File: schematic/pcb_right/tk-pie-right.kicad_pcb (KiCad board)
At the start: 2 copper layers, 129 x 77.5 mm, 26 parts, among them J1 UART, J2 DBG

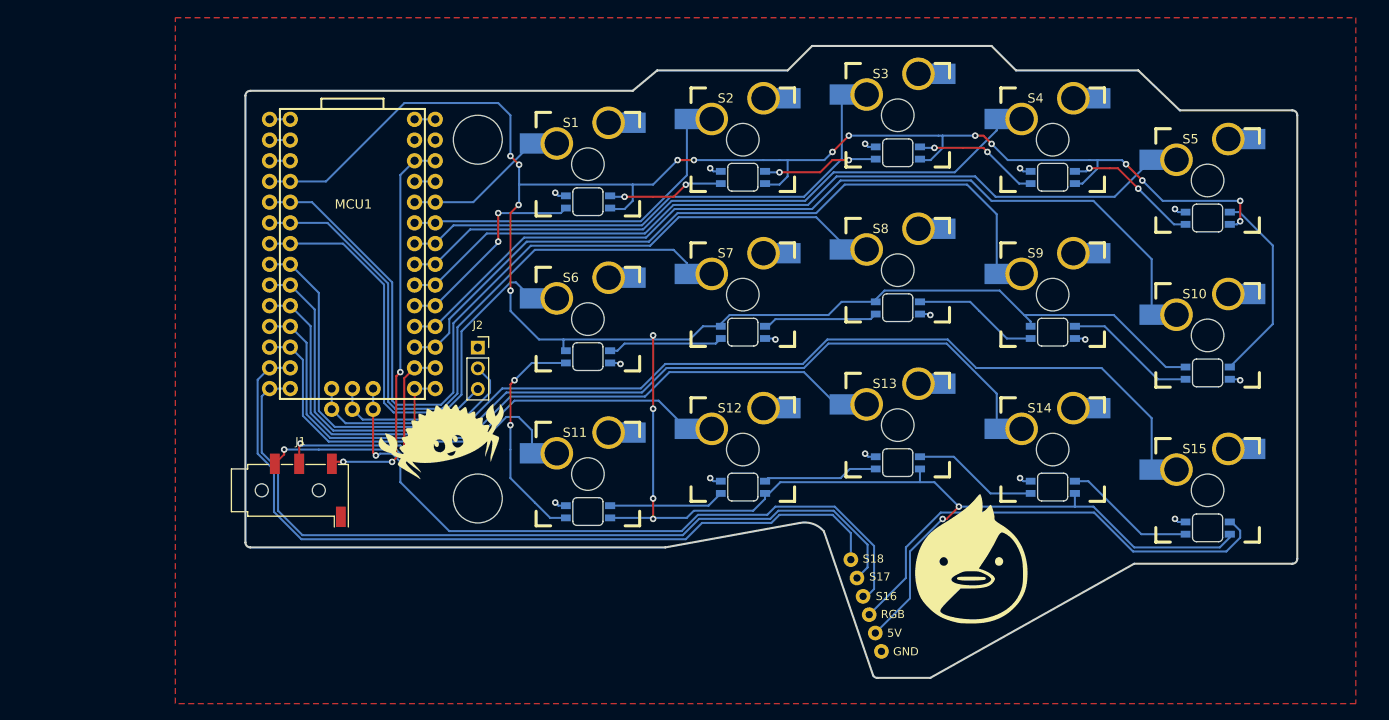
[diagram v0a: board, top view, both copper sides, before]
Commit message: Copy tk-pie-left to right and auto-flip it
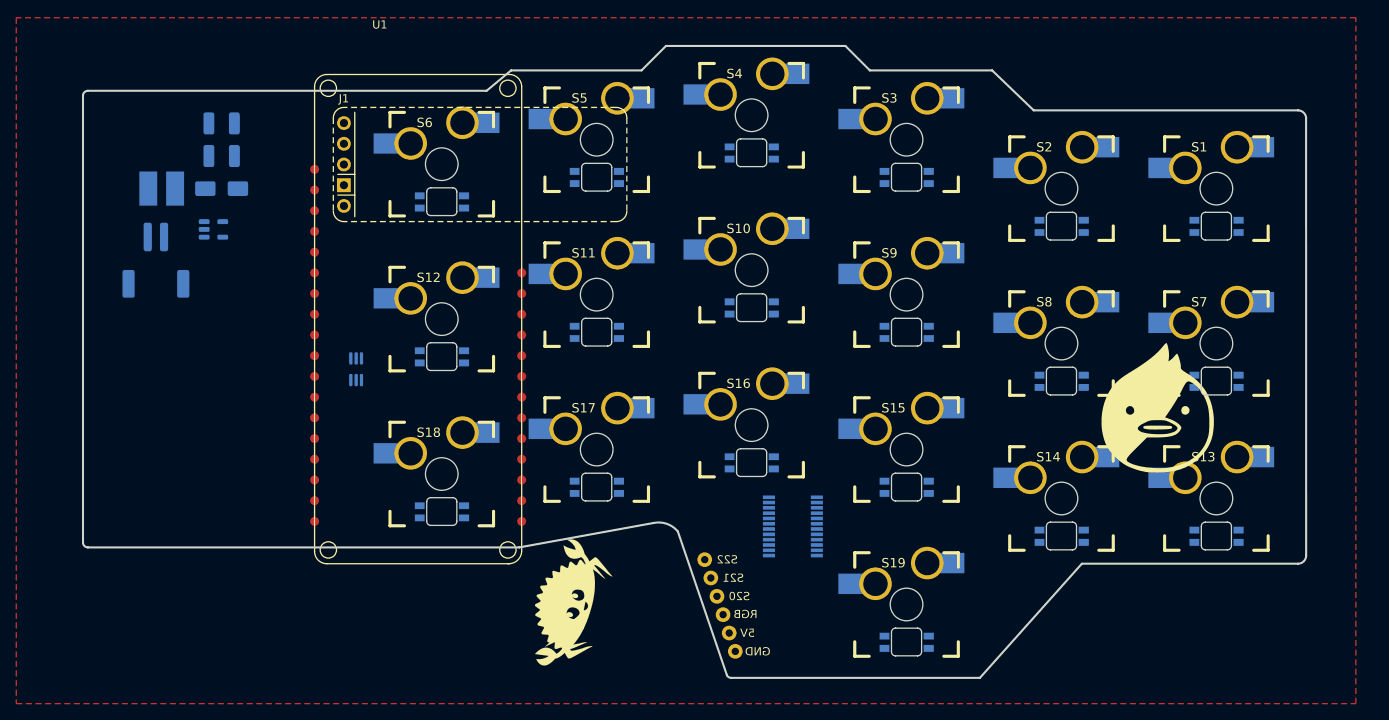
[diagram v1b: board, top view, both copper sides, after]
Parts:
- removed MCU1: ITSYBITSY RP2040, Footprints:ITSYBITSY BREAKOUT
- removed REF** (x2): MountingHole_6mm, MountingHole:MountingHole_6mm
- added C4: 12µF, Capacitor_SMD:C_1210_3225Metric_Pad1.33x2.70mm_HandSolder, B.Cu at (25.1, 35.0)
- added C5: 12µF, Capacitor_SMD:C_1210_3225Metric_Pad1.33x2.70mm_HandSolder, B.Cu at (25.1, 31.0)
- added D1: SS14, Diode_SMD:D_SMA, B.Cu at (25.1, 39.0)
- added IC1: PCA9539PW,118, Footprints:SOP65P640X110-24N, B.Cu at (95.1, 80.4)
- added L2: 22µH, Inductor_SMD:L_Cenker_CKCS5040, B.Cu at (17.7, 39.0)
- added PS1: ME2108C50M5G, Package_TO_SOT_SMD:SOT-23-5, B.Cu at (24.1, 44.0)
- added S1: MX_SW_SOCKET_LED, Footprints:MX_SW_SOCKET_LED, F.Cu at (147.1, 39.0)
- added S13: MX_SW_SOCKET_LED, Footprints:MX_SW_SOCKET_LED, F.Cu at (147.1, 77.0)
- added S19: MX_SW_SOCKET_RGB_REV, Footprints:MX_SW_SOCKET_LED_REV, F.Cu at (109.1, 90.0)
- added S7: MX_SW_SOCKET_RGB_REV, Footprints:MX_SW_SOCKET_LED_REV, F.Cu at (147.1, 58.0)
- added U1: ~, Footprints:DFR1075, F.Cu at (36.5, 25.0)
- added U3: SN74LVC1T45DCK, Package_TO_SOT_SMD:SOT-363_SC-70-6_Handsoldering, B.Cu at (41.6, 61.1)
- J1: value UART -> NiceView; footprint Connector_Audio:Jack_3.5mm_KoreanHropartsElec_PJ-320D-4A_Horizontal -> Footprints:Nice!View Header
- J2: value DBG -> Battery Connector; footprint Connector_PinSocket_2.54mm:PinSocket_1x03_P2.54mm_Vertical -> Connector_JST:JST_PH_S2B-PH-SM4-TB_1x02-1MP_P2.00mm_Horizontal; moved to B.Cu
- S10: renamed from S8; footprint Footprints:MX_SW_SOCKET_LED -> Footprints:MX_SW_SOCKET_LED_REV
- S11: renamed from S9; footprint Footprints:MX_SW_SOCKET_LED -> Footprints:MX_SW_SOCKET_LED_REV
- S12: renamed from S10; footprint Footprints:MX_SW_SOCKET_LED -> Footprints:MX_SW_SOCKET_LED_REV
- S14: renamed from S11; footprint Footprints:MX_SW_SOCKET_LED_REV -> Footprints:MX_SW_SOCKET_LED
- S15: renamed from S12; footprint Footprints:MX_SW_SOCKET_LED_REV -> Footprints:MX_SW_SOCKET_LED
- S16: renamed from S13; footprint Footprints:MX_SW_SOCKET_LED_REV -> Footprints:MX_SW_SOCKET_LED
- S17: renamed from S14; footprint Footprints:MX_SW_SOCKET_LED_REV -> Footprints:MX_SW_SOCKET_LED
- S18: renamed from S15; footprint Footprints:MX_SW_SOCKET_LED_REV -> Footprints:MX_SW_SOCKET_LED
- S2: renamed from S1; footprint Footprints:MX_SW_SOCKET_LED_REV -> Footprints:MX_SW_SOCKET_LED
- S3: renamed from S2; footprint Footprints:MX_SW_SOCKET_LED_REV -> Footprints:MX_SW_SOCKET_LED
- S4: renamed from S3; footprint Footprints:MX_SW_SOCKET_LED_REV -> Footprints:MX_SW_SOCKET_LED
- S5: renamed from S4; footprint Footprints:MX_SW_SOCKET_LED_REV -> Footprints:MX_SW_SOCKET_LED
- S6: renamed from S5; footprint Footprints:MX_SW_SOCKET_LED_REV -> Footprints:MX_SW_SOCKET_LED
- S8: renamed from S6; footprint Footprints:MX_SW_SOCKET_LED -> Footprints:MX_SW_SOCKET_LED_REV
- S9: renamed from S7; footprint Footprints:MX_SW_SOCKET_LED -> Footprints:MX_SW_SOCKET_LED_REV
- moved S12 93.9 mm to (52.1, 55.0)
- moved S18 93.9 mm to (52.1, 74.0)
- moved S6 93.9 mm to (52.1, 36.0)
- moved S14 58.2 mm to (128.1, 77.0)
- moved S2 58.2 mm to (128.1, 39.0)
- moved S8 58.2 mm to (128.1, 58.0)
- moved S11 55.9 mm to (71.1, 52.0)
- moved S17 55.9 mm to (71.1, 71.0)
- moved S5 55.9 mm to (71.1, 33.0)
- moved J1 45.4 mm to (40.1, 31.0)
- moved J2 40.9 mm to (17.0, 47.8), turned to 180 degrees
- moved S15 20.1 mm to (109.1, 71.0)
- moved S3 20.1 mm to (109.1, 33.0)
- moved S9 20.1 mm to (109.1, 52.0)
- moved E1 17.9 mm to (88.1, 95.8)
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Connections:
- E4 pad 1: /S16 -> /S20
- E5 pad 1: /S17 -> /S21
- E6 pad 1: /S18 -> /S22
- J2 pad 1: GND -> /VBAT
- J2 pad 2: Net-(J2-Pin_2) -> GND
- S10 pad 1: /S8 -> GND
- S10 pad 2: GND -> /S10
- S10 pad 5: Net-(S8-DIN) -> Net-(S10-DIN)
- S10 pad 6: Net-(S7-DIN) -> Net-(S10-DOUT)
- S11 pad 1: /S9 -> GND
- S11 pad 2: GND -> /S11
- S11 pad 6: Net-(S8-DIN) -> Net-(S11-DOUT)
- S12 pad 1: /S10 -> GND
- S12 pad 2: GND -> /S12
- S12 pad 5: Net-(S10-DIN) -> Net-(S11-DOUT)
- S12 pad 6: Net-(S10-DOUT) -> Net-(S12-DOUT)
- S14 pad 1: /S11 -> GND
- S14 pad 2: GND -> /S14
- S14 pad 5: Net-(S11-DIN) -> Net-(S14-DIN)
- S14 pad 6: Net-(S11-DOUT) -> Net-(S13-DIN)
- S15 pad 1: /S12 -> GND
- S15 pad 2: GND -> /S15
- S15 pad 5: Net-(S11-DOUT) -> Net-(S15-DIN)
- S15 pad 6: Net-(S12-DOUT) -> Net-(S14-DIN)
- S16 pad 1: /S13 -> GND
- S16 pad 2: GND -> /S16
- S16 pad 5: Net-(S12-DOUT) -> Net-(S16-DIN)
- S16 pad 6: Net-(S13-DOUT) -> Net-(S15-DIN)
- S17 pad 1: /S14 -> GND
- S17 pad 2: GND -> /S17
- S17 pad 5: Net-(S13-DOUT) -> Net-(S17-DIN)
- S17 pad 6: Net-(S14-DOUT) -> Net-(S16-DIN)
- S18 pad 1: /S15 -> GND
- S18 pad 2: GND -> /S18
- S18 pad 5: Net-(S14-DOUT) -> Net-(S12-DOUT)
- S18 pad 6: Net-(E3-Pin_1) -> Net-(S17-DIN)
- S2 pad 1: /S1 -> GND
- S2 pad 2: GND -> /S2
- S2 pad 5: /NEOPIXEL_DIN -> Net-(S2-DIN)
- S2 pad 6: Net-(S1-DOUT) -> Net-(S1-DIN)
- S3 pad 1: /S2 -> GND
- S3 pad 2: GND -> /S3
- S3 pad 5: Net-(S1-DOUT) -> Net-(S3-DIN)
- S3 pad 6: Net-(S2-DOUT) -> Net-(S2-DIN)
- S4 pad 1: /S3 -> GND
- S4 pad 2: GND -> /S4
- S4 pad 5: Net-(S2-DOUT) -> Net-(S4-DIN)
- S4 pad 6: Net-(S3-DOUT) -> Net-(S3-DIN)
- S5 pad 1: /S4 -> GND
- S5 pad 2: GND -> /S5
- S5 pad 5: Net-(S3-DOUT) -> Net-(S5-DIN)
- S5 pad 6: Net-(S4-DOUT) -> Net-(S4-DIN)
- S6 pad 1: /S5 -> GND
- S6 pad 2: GND -> /S6
- S6 pad 5: Net-(S4-DOUT) -> /NEOPIXEL_DIN
- S6 pad 6: Net-(S10-DIN) -> Net-(S5-DIN)
- S8 pad 1: /S6 -> GND
- S8 pad 2: GND -> /S8
- S8 pad 5: Net-(S6-DIN) -> Net-(S7-DOUT)
- S8 pad 6: Net-(S11-DIN) -> Net-(S8-DOUT)
- S9 pad 1: /S7 -> GND
- S9 pad 2: GND -> /S9
- S9 pad 5: Net-(S7-DIN) -> Net-(S8-DOUT)
- S9 pad 6: Net-(S6-DIN) -> Net-(S10-DIN)
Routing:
- net +5V: track 400.1 -> 0.00 mm, vias 20 -> 0
- net /S15: track 139.7 -> 0.00 mm
- net /S14: track 115.2 -> 0.00 mm
- net /S10: track 108.6 -> 0.00 mm
- net /S8: track 105.6 -> 0.00 mm
- net /S17: track 99.9 -> 0.00 mm
- net /S18: track 99.2 -> 0.00 mm
- net /S5: track 98.8 -> 0.00 mm
- net /S9: track 89.5 -> 0.00 mm
- net /S13: track 87.8 -> 0.00 mm
- net /S16: track 84.7 -> 0.00 mm, vias 1 -> 0
- net /S7: track 84.0 -> 0.00 mm
- net /S4: track 79.6 -> 0.00 mm
- net /S12: track 65.3 -> 0.00 mm
- net /S3: track 64.6 -> 0.00 mm
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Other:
- board size 129 x 77.5 mm -> 150 x 77.5 mm
- board text added: "S20"
- board text added: "S21"
- board text added: "S22"
- board text removed: "S16"
- board text removed: "S17"
- board text removed: "S18"

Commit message: pcb_right: Fix mcu position
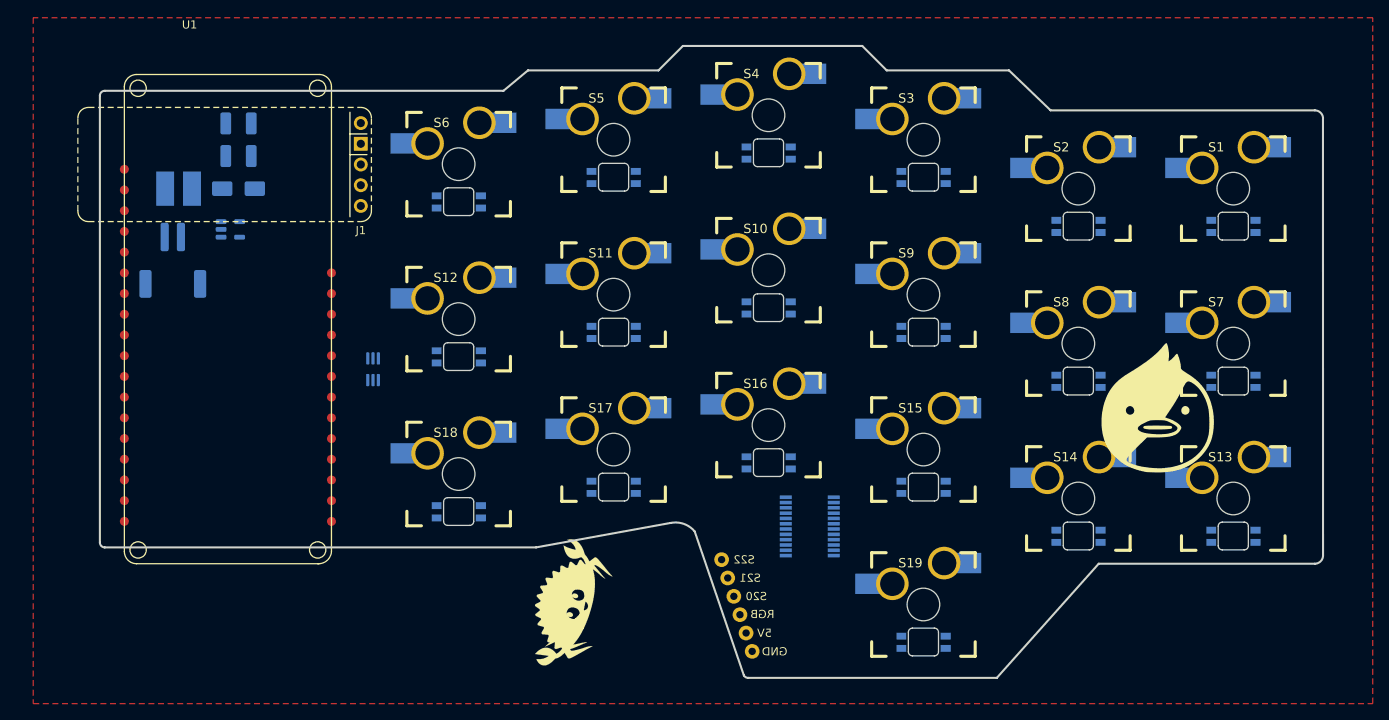
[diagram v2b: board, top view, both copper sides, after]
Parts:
- moved U1 31.8 mm to (25.9, 55.0)
- moved J1 10.4 mm to (42.1, 41.1), turned to 180 degrees
- moved E1 2.07 mm to (90.2, 95.8)
- moved E2 2.07 mm to (89.4, 93.5)
- moved E3 2.07 mm to (88.7, 91.2)
- moved E4 2.07 mm to (87.9, 89.0)
- moved E5 2.07 mm to (87.2, 86.8)
- moved E6 2.07 mm to (86.4, 84.5)
- moved IC1 2.07 mm to (97.2, 80.4)
- moved S10 2.07 mm to (92.2, 49.0)
- moved S11 2.07 mm to (73.2, 52.0)
- moved S15 2.07 mm to (111.2, 71.0)
- moved S16 2.07 mm to (92.2, 68.0)
- moved S17 2.07 mm to (73.2, 71.0)
- moved S19 2.07 mm to (111.2, 90.0)
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
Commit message: RIGHT PCB ???? TRACES VIAS!!!!
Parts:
- S1, S13, S4, S5, S6: value MX_SW_SOCKET_LED -> MX_SW_SOCKET_RGB_REV; footprint Footprints:MX_SW_SOCKET_LED -> Footprints:MX_SW_SOCKET_LED_REV
- S10, S11, S12, S19, S7, S8, S9: value MX_SW_SOCKET_RGB_REV -> MX_SW_SOCKET_LED; footprint Footprints:MX_SW_SOCKET_LED_REV -> Footprints:MX_SW_SOCKET_LED
- S14, S15, S16, S17, S18, S2, S3: value ~ -> MX_SW_SOCKET_RGB_REV; footprint Footprints:MX_SW_SOCKET_LED -> Footprints:MX_SW_SOCKET_LED_REV
- turned C4 to 180 degrees
- turned C5 to 0 degrees
- turned D1 to 180 degrees
- turned IC1 to 180 degrees
- turned L2 to 0 degrees
- turned PS1 to 180 degrees
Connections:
- IC1 pad 10: /S2 -> /S14
- IC1 pad 11: /S15 -> /S19
- IC1 pad 13: /S3 -> /S20
- IC1 pad 14: /S9 -> /S21
- IC1 pad 15: /S16 -> /S22
- IC1 pad 16: /S10 -> /S4
- IC1 pad 17: /S4 -> /S10
- IC1 pad 18: /S22 -> /S16
- IC1 pad 19: /S21 -> /S9
- IC1 pad 20: /S20 -> /S3
- IC1 pad 24: +5V -> +3.3V
- IC1 pad 4: /S19 -> /S15
- IC1 pad 5: /S14 -> /S2
- IC1 pad 6: /S13 -> /S1
- IC1 pad 7: /S7 -> /S8
- IC1 pad 8: /S1 -> /S7
- IC1 pad 9: /S8 -> /S13
- S1 pad 1: GND -> /S1
- S1 pad 2: /S1 -> GND
- S10 pad 1: GND -> /S10
- S10 pad 2: /S10 -> GND
- S11 pad 1: GND -> /S11
- S11 pad 2: /S11 -> GND
- S12 pad 1: GND -> /S12
- S12 pad 2: /S12 -> GND
- S13 pad 1: GND -> /S13
- S13 pad 2: /S13 -> GND
- S14 pad 1: GND -> /S14
- S14 pad 2: /S14 -> GND
- S15 pad 1: GND -> /S15
- S15 pad 2: /S15 -> GND
- S16 pad 1: GND -> /S16
- S16 pad 2: /S16 -> GND
- S17 pad 1: GND -> /S17
- S17 pad 2: /S17 -> GND
- S18 pad 1: GND -> /S18
- S18 pad 2: /S18 -> GND
- S19 pad 1: GND -> /S19
- S19 pad 2: /S19 -> GND
- S2 pad 1: GND -> /S2
- S2 pad 2: /S2 -> GND
- S3 pad 1: GND -> /S3
- S3 pad 2: /S3 -> GND
- S4 pad 1: GND -> /S4
- S4 pad 2: /S4 -> GND
- S5 pad 1: GND -> /S5
- S5 pad 2: /S5 -> GND
- S6 pad 1: GND -> /S6
- S6 pad 2: /S6 -> GND
- S7 pad 1: GND -> /S7
- S7 pad 2: /S7 -> GND
- S8 pad 1: GND -> /S8
- S8 pad 2: /S8 -> GND
- S9 pad 1: GND -> /S9
- S9 pad 2: /S9 -> GND
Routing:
- net +5V: track 0.00 -> 494.6 mm, vias 0 -> 47
- net +3.3V: track 0.00 -> 134.1 mm, vias 0 -> 21
- net /GPIOE_RST: track 0.00 -> 81.7 mm, vias 0 -> 5
- net /S1: track 0.00 -> 78.7 mm
- net /GPIOE_INT: track 0.00 -> 77.3 mm, vias 0 -> 7
- net /S5: track 0.00 -> 77.2 mm, vias 0 -> 5
- net /S4: track 0.00 -> 68.9 mm
- net /S11: track 0.00 -> 67.9 mm, vias 0 -> 3
- net /S2: track 0.00 -> 64.1 mm
- net /S7: track 0.00 -> 61.4 mm
- net /GPIOE_SDA: track 0.00 -> 59.7 mm, vias 0 -> 3
- net /S17: track 0.00 -> 59.5 mm, vias 0 -> 1
- net /GPIOE_SCL: track 0.00 -> 59.3 mm, vias 0 -> 3
- net /S13: track 0.00 -> 58.8 mm
- net /S3: track 0.00 -> 56.2 mm
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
